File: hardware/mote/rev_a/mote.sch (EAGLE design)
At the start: 107 parts, among them J1 TC2030-JLINK-L, Q10 CSD22206W, Q11 CSD22206W, Q6 CSD22206W, Q7 CSD22206W, Q8 CSD22206W, Q9 CSD22206W, U1 NRF52840, U10 MS5637-02BA03, U11 ADP5091, U3 MAX17222, U4 AMN41121, U5 SI7021-A20-GM1, U6 ISL29125, U7 MAX44009, U8 LIS2DW12, U9 AB1815-T3, X1 7V-32.000MAHV-T, X3 ABS07-32.768KHZ-7-T

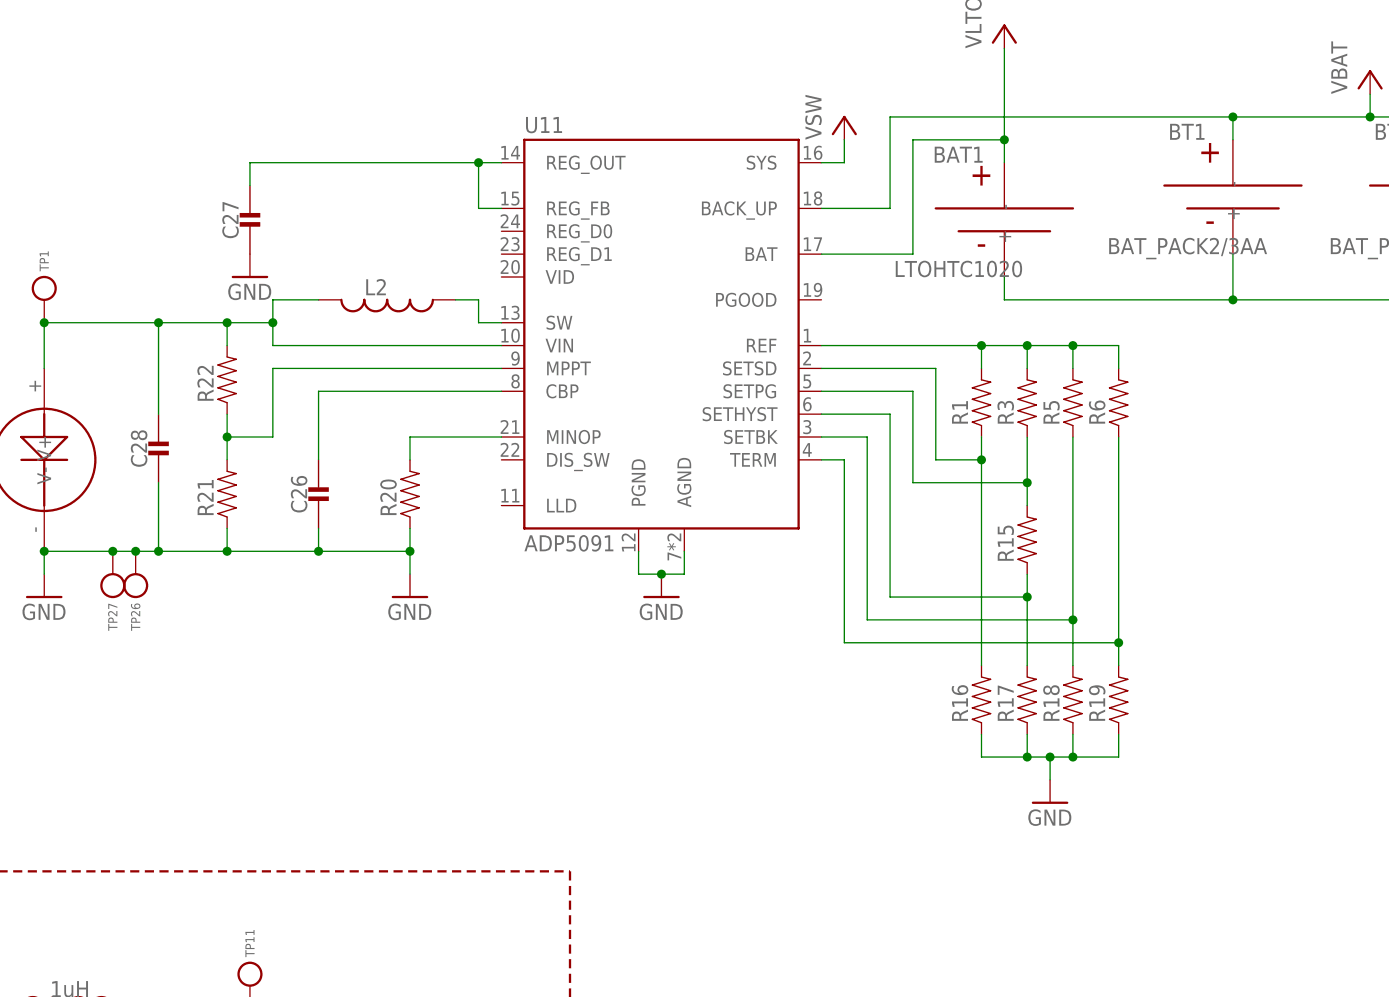
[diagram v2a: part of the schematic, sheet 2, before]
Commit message: add component values for mppt
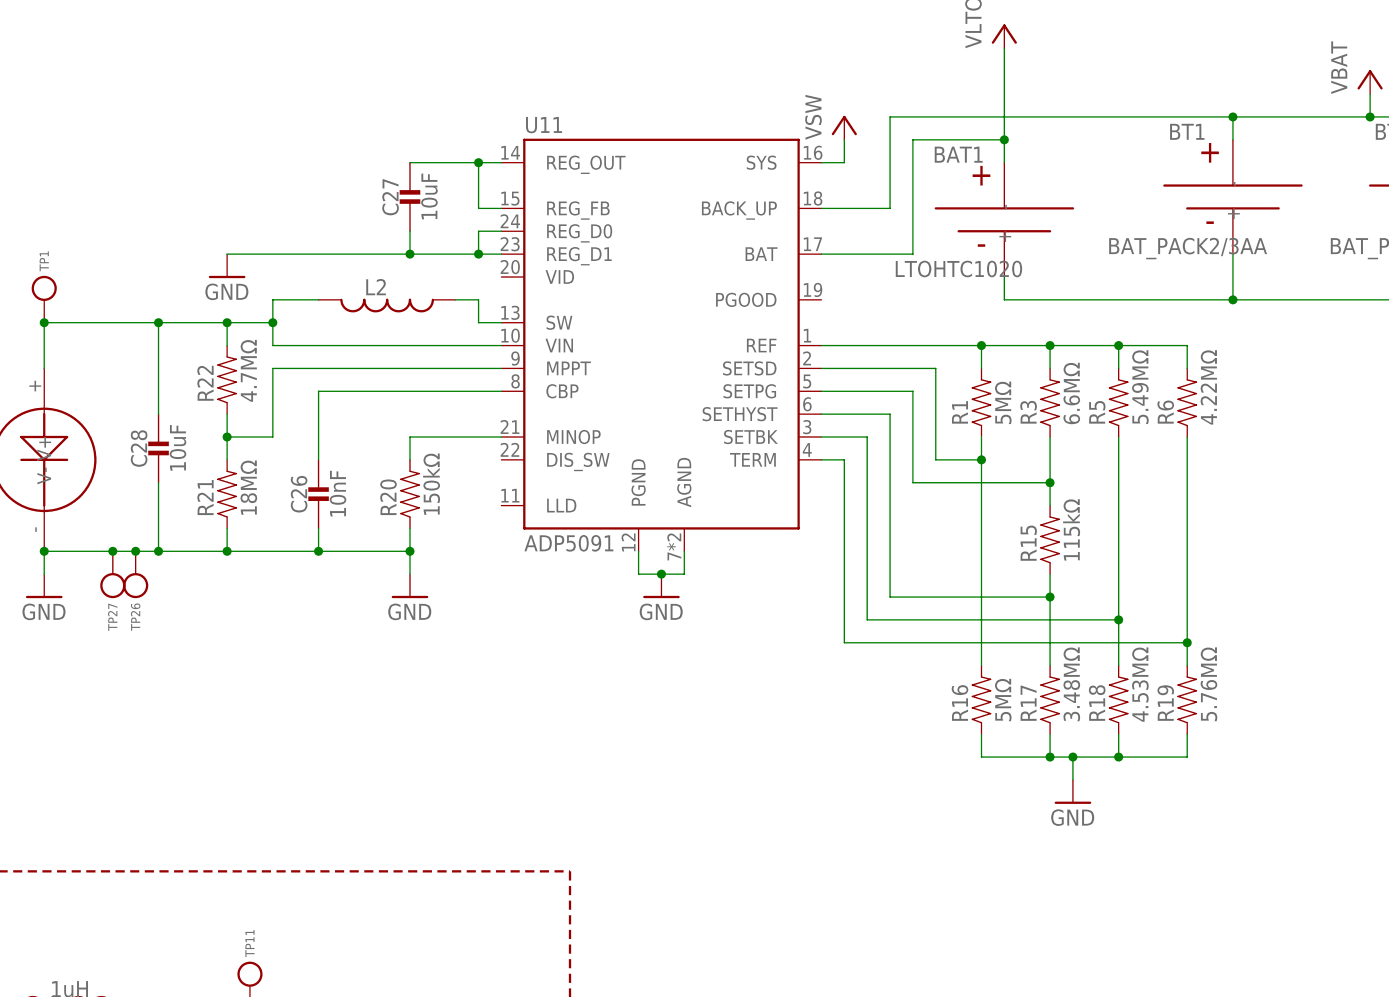
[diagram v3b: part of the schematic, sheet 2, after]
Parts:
- C26: value (none) -> 10nF
- C27, C28: value (none) -> 10uF
- R1, R16: value (none) -> 5MΩ
- R15: value (none) -> 115kΩ
- R17: value (none) -> 3.48MΩ
- R18: value (none) -> 4.53MΩ
- R19: value (none) -> 5.76MΩ
- R20: value (none) -> 150kΩ
- R21: value (none) -> 18MΩ
- R22: value (none) -> 4.7MΩ
- R3: value (none) -> 6.6MΩ
- R5: value (none) -> 5.49MΩ
- R6: value (none) -> 4.22MΩ
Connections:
- net GND: now also U11.REG_D0, U11.REG_D1
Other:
- moved on the sheet: C27, R15, R17, R18, R19, R3, R5, R6

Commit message: small visual changes
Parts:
- L2: value (none) -> 22uH
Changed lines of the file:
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@@
 <part name="R21" library="passives" deviceset="RESISTOR" device="0402_RES" value="18MΩ"/>
 <part name="R22" library="passives" deviceset="RESISTOR" device="0402_RES" value="4.7MΩ"/>
-<part name="L2" library="passives" deviceset="INDUCTOR" device="IHL2525CZ">
+<part name="L2" library="passives" deviceset="INDUCTOR" device="IHL2525CZ" value="22uH">
 <attribute name="DIGIKEY" value="541-2562-1-ND"/>
 </part>
@@
 <wire x1="88.9" y1="109.22" x2="88.9" y2="175.26" width="0.254" layer="94" style="shortdash"/>
 <text x="5.08" y="170.18" size="2.54" layer="95">Accelerometer</text>
-<text x="60.96" y="104.14" size="2.54" layer="95" align="bottom-center">Temperature</text>
+<text x="63.5" y="104.14" size="2.54" layer="95" align="bottom-center">Temperature</text>
 <text x="68.58" y="96.52" size="2.54" layer="95">Humidity</text>
 <text x="2.54" y="96.52" size="2.54" layer="95">Pressure</text>
@@
 <text x="91.44" y="170.18" size="2.54" layer="95">Light Color</text>
 <wire x1="88.9" y1="175.26" x2="0" y2="175.26" width="0.254" layer="94" style="shortdash"/>
-<wire x1="88.9" y1="175.26" x2="144.78" y2="175.26" width="0.254" layer="94" style="shortdash"/>
-<wire x1="144.78" y1="175.26" x2="205.74" y2="175.26" width="0.254" layer="94" style="shortdash"/>
+<wire x1="88.9" y1="175.26" x2="147.32" y2="175.26" width="0.254" layer="94" style="shortdash"/>
+<wire x1="147.32" y1="175.26" x2="205.74" y2="175.26" width="0.254" layer="94" style="shortdash"/>
 <wire x1="205.74" y1="175.26" x2="205.74" y2="109.22" width="0.254" layer="94" style="shortdash"/>
-<wire x1="205.74" y1="109.22" x2="144.78" y2="109.22" width="0.254" layer="94" style="shortdash"/>
-<wire x1="144.78" y1="109.22" x2="132.08" y2="109.22" width="0.254" layer="94" style="shortdash"/>
+<wire x1="205.74" y1="109.22" x2="147.32" y2="109.22" width="0.254" layer="94" style="shortdash"/>
+<wire x1="147.32" y1="109.22" x2="129.54" y2="109.22" width="0.254" layer="94" style="shortdash"/>
 <wire x1="129.54" y1="109.22" x2="88.9" y2="109.22" width="0.254" layer="94" style="shortdash"/>
-<wire x1="144.78" y1="175.26" x2="144.78" y2="109.22" width="0.254" layer="94" style="shortdash"/>
-<wire x1="0" y1="45.72" x2="66.04" y2="45.72" width="0.254" layer="94" style="shortdash"/>
-<wire x1="66.04" y1="45.72" x2="129.54" y2="45.72" width="0.254" layer="94" style="shortdash"/>
+<wire x1="147.32" y1="175.26" x2="147.32" y2="109.22" width="0.254" layer="94" style="shortdash"/>
+<wire x1="0" y1="45.72" x2="63.5" y2="45.72" width="0.254" layer="94" style="shortdash"/>
+<wire x1="63.5" y1="45.72" x2="129.54" y2="45.72" width="0.254" layer="94" style="shortdash"/>
 <wire x1="129.54" y1="45.72" x2="129.54" y2="101.6" width="0.254" layer="94" style="shortdash"/>
 <wire x1="129.54" y1="101.6" x2="129.54" y2="109.22" width="0.254" layer="94" style="shortdash"/>
-<wire x1="129.54" y1="109.22" x2="132.08" y2="109.22" width="0.254" layer="94" style="shortdash"/>
-<wire x1="66.04" y1="45.72" x2="66.04" y2="101.6" width="0.254" layer="94" style="shortdash"/>
-<wire x1="66.04" y1="101.6" x2="129.54" y2="101.6" width="0.254" layer="94" style="shortdash"/>
-<wire x1="66.04" y1="101.6" x2="0" y2="101.6" width="0.254" layer="94" style="shortdash"/>
-<text x="144.78" y="177.8" size="2.54" layer="95" align="bottom-center">Light</text>
+<wire x1="63.5" y1="45.72" x2="63.5" y2="101.6" width="0.254" layer="94" style="shortdash"/>
+<wire x1="63.5" y1="101.6" x2="129.54" y2="101.6" width="0.254" layer="94" style="shortdash"/>
+<wire x1="63.5" y1="101.6" x2="0" y2="101.6" width="0.254" layer="94" style="shortdash"/>
+<text x="147.32" y="177.8" size="2.54" layer="95" align="bottom-center">Light</text>
 <wire x1="88.9" y1="175.26" x2="88.9" y2="182.88" width="0.254" layer="94" style="shortdash"/>
 <wire x1="88.9" y1="182.88" x2="205.74" y2="182.88" width="0.254" layer="94" style="shortdash"/>

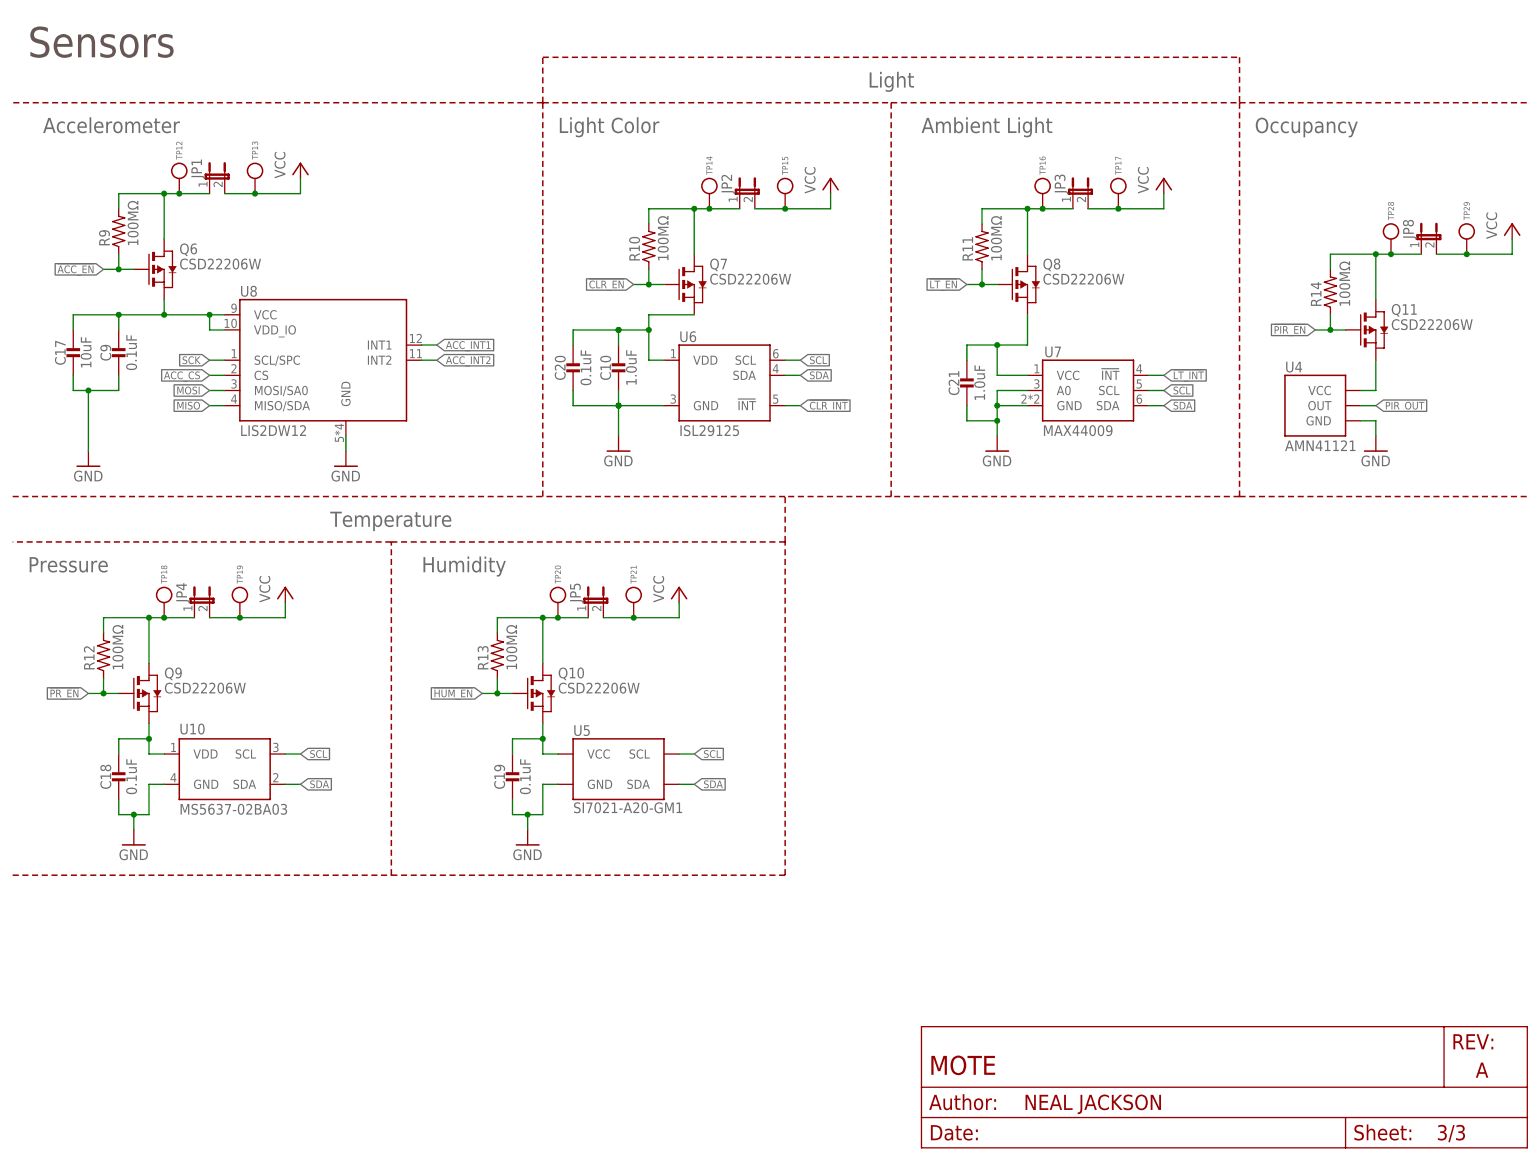
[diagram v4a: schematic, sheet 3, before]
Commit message: Fix some issues from design review
See #1

adc to vsw
reverse power gate fets
decoup caps before fet
pullups on interrupts
gate i2c
enable dc-dc mode for dcc
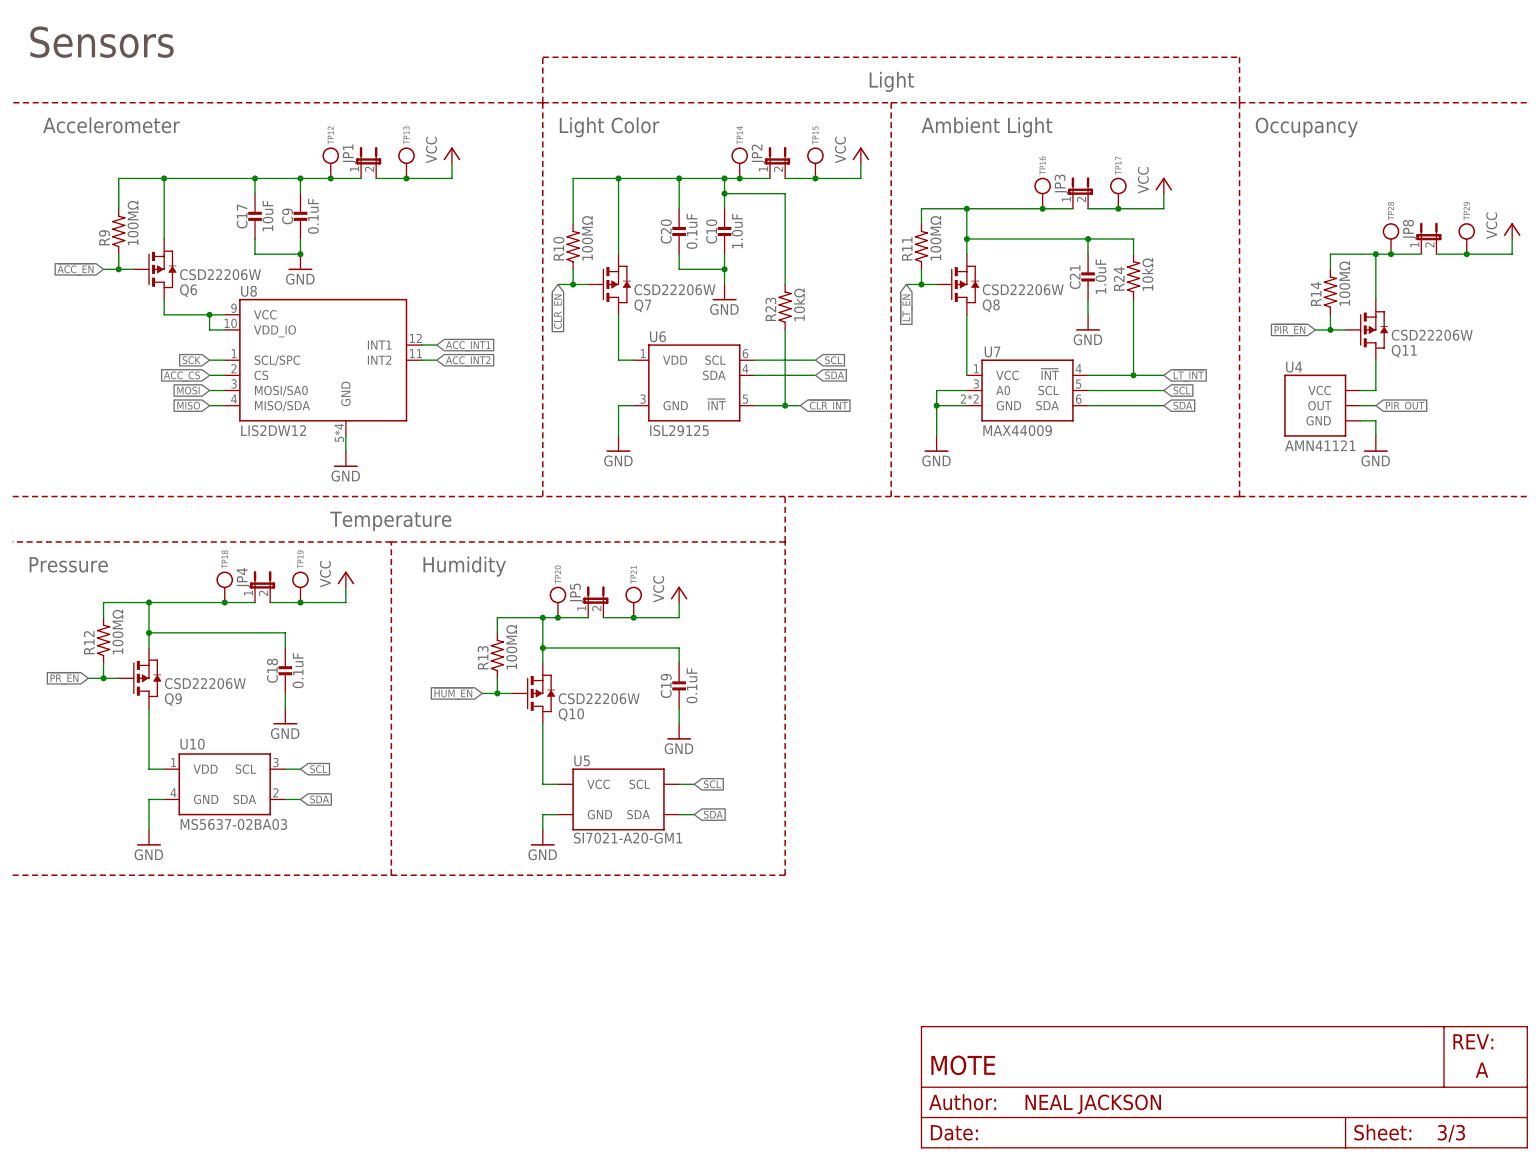
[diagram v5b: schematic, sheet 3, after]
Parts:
- added C29: 47nF, passives:CAPACITOR0402_CAP
- added L4: 10uH, passives:INDUCTORIHL2525CZ
- added L5: 15nH, passives:INDUCTORIHL2525CZ
- added Q1, Q2: CSD22206W, fets:CSD22206W
- added R23, R24: 10kΩ, passives:RESISTOR0402_RES
- added R25: 100MΩ, passives:RESISTOR0402_RES
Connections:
- removed net N$35: JP4.1, Q9.D, R12.2, TP18.TESTPOINT
- new net !I2C_EN: Q1.G, Q2.G, R25.1, U1.P1.09
- new net N$31: Q7.D, U6.VDD
- new net N$40: C17.1, C9.1, JP1.1, Q6.S, R9.2, TP12.TESTPOINT
- new net N$41: Q1.D, R8.2
- new net N$44: L4.2, U1.DCC
- new net N$46: L4.1, L5.2
- net !CLR_INT: now also R23.1
- net !LT_INT: now also R24.1
- net GND: now also C29.2
- net N$15: now also Q6.D; no longer C17.1, C9.1, Q6.S
- net N$19: now also C18.1, JP4.1, Q9.S, R12.2, TP18.TESTPOINT; no longer C10.1, C20.1, Q7.S, U6.VDD
- net N$20: now also Q8.D; no longer C21.1, Q8.S
- net N$21: now also Q9.D; no longer C18.1, Q9.S
- net N$22: now also Q10.D; no longer C19.1, Q10.S
- net N$23: now also Q11.D; no longer Q11.S
- net N$24: now also Q11.S; no longer Q11.D
- net N$3: now also C29.1, L5.1, U1.DEC6
- net N$33: now also C10.1, C20.1, Q7.S, R23.2; no longer Q7.D
- net N$34: now also Q2.D, R7.2; no longer JP3.1, Q8.D, R11.2, TP16.TESTPOINT
- net N$36: now also C19.1, Q10.S; no longer Q10.D
- net N$37: now also C21.1, JP3.1, Q8.S, R11.2, R24.2, TP16.TESTPOINT; no longer JP1.1, Q6.D, R9.2, TP12.TESTPOINT
- net PIR_OUT: no longer U1.P1.09
- net SW: now also U1.P0.04/AIN2
- net VCC: now also Q1.S, Q2.S, R25.2; no longer R7.2, R8.2
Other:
- moved on the sheet: C10, C11, C15, C17, C18, C19, C20, C21, C5, C9, JP1, JP2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

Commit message: add NRF51822
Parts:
- removed L4: 10uH, passives:INDUCTORIHL2525CZ
- removed L5: 15nH, passives:INDUCTORIHL2525CZ
- added A3: FRACTUS-2.4GHZ-FR05-S1-N-0-102, chips:FRACTUS-2.4GHZ-FR05-S1-N-0-102
- added B2: BAL-NRF01D3, chips:BAL-NRF01D3
- added C30, C31, C46, C47, C52, C53: 12pF, passives:CAPACITOR0402_CAP
- added C42: 0.1uF, passives:CAPACITOR0402_CAP
- added C43, C48: 1nF, passives:CAPACITOR0402_CAP
- added C44: 4.7uF, passives:CAPACITOR0402_CAP
- added C45: 1uF, passives:CAPACITOR0402_CAP
- added C49: 47nF, passives:CAPACITOR0402_CAP
- added C50: 2.2nF, passives:CAPACITOR0402_CAP
- added C51: 0.8pF, passives:CAPACITOR0402_CAP
- added J2: TC2030-JLINK-NL, connector:TC2030-JLINK-NL
- added L6, L8: 15nH, passives:INDUCTOR0402
- added L7, L9: 10uH, passives:INDUCTOR0603
- added R29: 12k, passives:RESISTOR0402_RES
- added U12: NRF51822QF, chips:NRF51822QF
- added X2, X6: ABS05-32.768KHZ-9-T, crystals:ABS05-32.768KHZ-9-T
- added X5: 16MHz, crystals:TXC-8Y
- A1: value (none) -> FRACTUS-2.4GHZ-FR05-S1-N-0-102; device chips:AH212M -> chips:FRACTUS-2.4GHZ-FR05-S1-N-0-102
- C29: DIGIKEY 490-7195-1-ND -> 490-3254-1-ND
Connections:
- removed net N$46: L4.1, L5.2
- new net AVDD1: C43.1, C45.1, L8.1, U12.AVDD
- new net DCC1: L9.2, U12.DCC
- new net N$49: L6.2, L7.1
- new net N$60: B2.ANT1, U12.ANT1
- new net N$61: B2.ANT2, U12.ANT2
- new net N$62: A3.ANTENNA, B2.SE, C51.1
- new net N$63: L8.2, L9.1
- new net N$64: C46.1, U12.XC1, X5.1
- new net N$65: C47.1, U12.XC2, X5.2
- new net N$66: C48.1, U12.DEC1
- new net N$67: C49.1, U12.DEC2
- new net NRF_A2: C53.1, U12.P27/AIN1/XL1, X6.2
- new net NRF_A3: C52.1, U12.P26/AIN0/XL2, X6.1
- new net NRF_SWDCLK: J2.SWDCLK, R29.1, U12.SWDCLK
- new net NRF_SWDIO/!RESET: J2.SWDIO, J2.SWO, U12.SWDIO/!RESET
- new net NRF_VCC: C42.1, C44.1, J2.VCC, U12.VDD
- new net VDD_PA1: B2.VDD_PA, C50.1, U12.VDD_PA
- new net VSEC: BAT1.+, U1.P0.02/AIN0, U11.BAT
- new net XL1: C31.2, U1.P0.00/XL1, X2.1
- new net XL2: C30.2, U1.P0.01/XL2, X2.2
- net !CLR_EN: now also U1.P0.20; no longer U1.P1.14
- net !CLR_INT: now also U1.P1.02; no longer U1.P1.05
- net !HUM_EN: now also U1.P0.12; no longer U1.P1.11
- net !I2C_EN: no longer U1.P1.09
- net !PR_EN: now also U1.P1.09; no longer U1.P1.12
- net !RST: now also J1.!RESET, U1.P0.17
- net ACC_CS: now also U1.P0.15; no longer U1.P0.17
- net ACC_INT2: now also U1.P0.09/NFC1; no longer U1.P1.07
- net CLKOUT: no longer U1.P0.00/XL1
- net GND: now also B2.GND, C30.1, C31.1, C42.2, C43.2, C44.2, C45.2, C46.2, C47.2, C48.2, C49.2, C50.2, C51.2, C52.2, C53.2, J2.GND, R29.2, U12.GND; no longer U1.P0.01/XL2
- net MISO: now also U1.P1.00; no longer U1.P0.15
- net MOSI: now also U1.P0.24; no longer U1.P0.14
- net N$3: now also L6.1; no longer L5.1
- net N$44: now also L7.2; no longer L4.2
- net PIR_OUT: now also U1.P1.01; no longer U1.P1.03
- net RTC_CS: now also U1.P0.13; no longer U1.P0.16
- net SCK: now also U1.P0.22; no longer U1.P0.13
- net SCL: now also U1.P0.08; no longer U1.P0.27
- net SDA: now also U1.P0.06; no longer U1.P0.26
- net SW: now also U1.P0.26; no longer U1.P0.24
- net VBAT: now also U1.P0.29/AIN5; no longer U1.P0.03/AIN1
- net VSW: no longer BAT1.+, U1.P0.02/AIN0, U11.BAT
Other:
- note added: "Auxillary NRF51822"
